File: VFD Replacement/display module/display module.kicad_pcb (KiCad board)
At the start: 2 copper layers, 51.9 x 11 mm, 98 parts, among them J1 Conn_01x08_Pin, J2 Conn_01x12_Pin

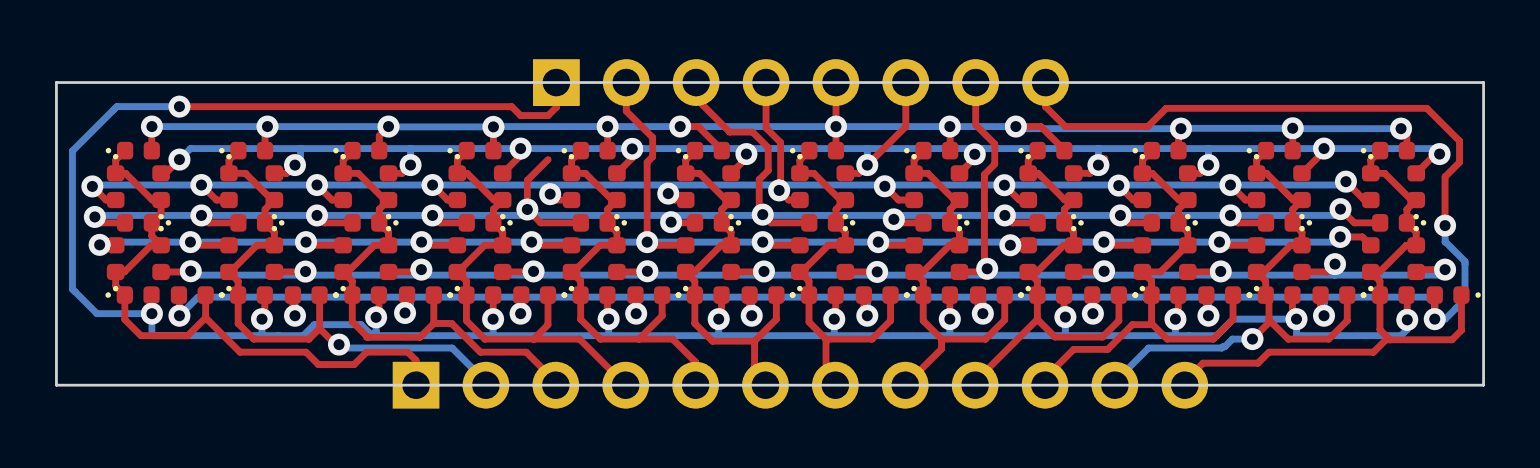
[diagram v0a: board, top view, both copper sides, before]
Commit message: Check 7-seg module and VFD interposer. Create outputs
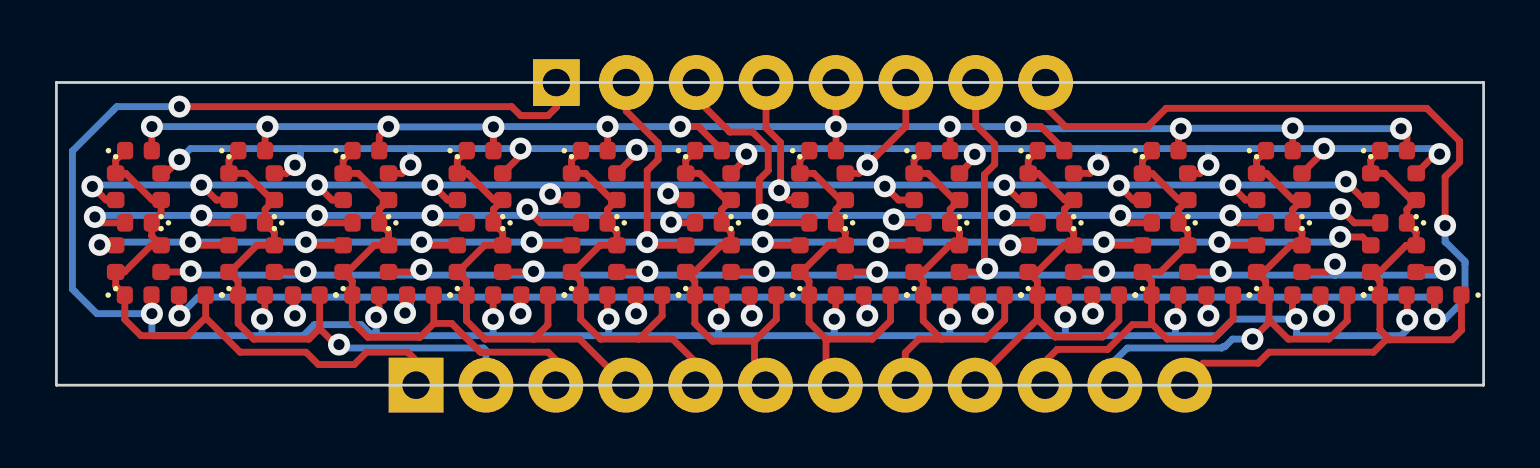
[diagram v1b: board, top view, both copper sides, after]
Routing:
- net /G: track 71.5 -> 69.3 mm
- net /G2: track 20.4 -> 21.1 mm

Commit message: Update outputs
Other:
- board text added: "7-seg LED Display Module"
- board text added: "JLCJLCJLCJLC"
- board text added: "V1.0"
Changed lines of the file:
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@@
   (gr_rect (start 130.928196 50.6) (end 182.8 61.6)
     (stroke (width 0.1) (type default)) (fill none) (layer "Edge.Cuts"))
+  (gr_text "V1.0" (at 168.1 56.4 0) (layer "B.SilkS")
+    (effects (font (size 1 1) (thickness 0.15)) (justify left bottom mirror))
+  )
+  (gr_text "JLCJLCJLCJLC" (at 136.8 60.7 0) (layer "B.SilkS")
+    (effects (font (size 0.8 0.2) (thickness 0.025)) (justify left bottom mirror))
+  )
+  (gr_text "7-seg LED Display Module" (at 168.4 54.8 0) (layer "B.SilkS")
+    (effects (font (size 1 1) (thickness 0.15)) (justify left bottom mirror))
+  )
   (segment (start 153.399169 54.87) (end 153.8 54.87) (width 0.25) (layer "F.Cu") (net 1))
   (segment (start 157.25 54.466875) (end 157.25 52.781299) (width 0.25) (layer "F.Cu") (net 1))
